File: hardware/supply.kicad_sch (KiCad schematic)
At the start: 13 parts, among them U4 LMR51610XDBVR

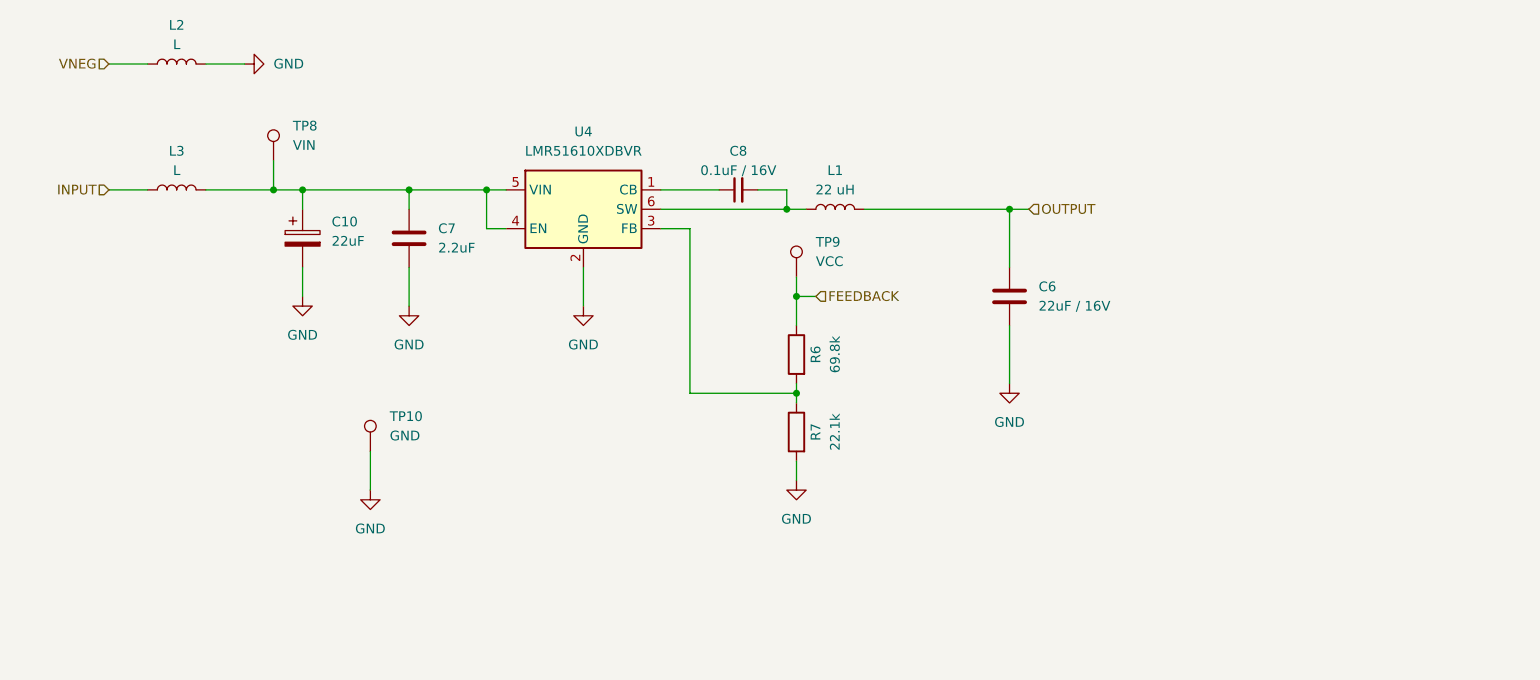
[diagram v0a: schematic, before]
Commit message: Remove PLC, use ESP
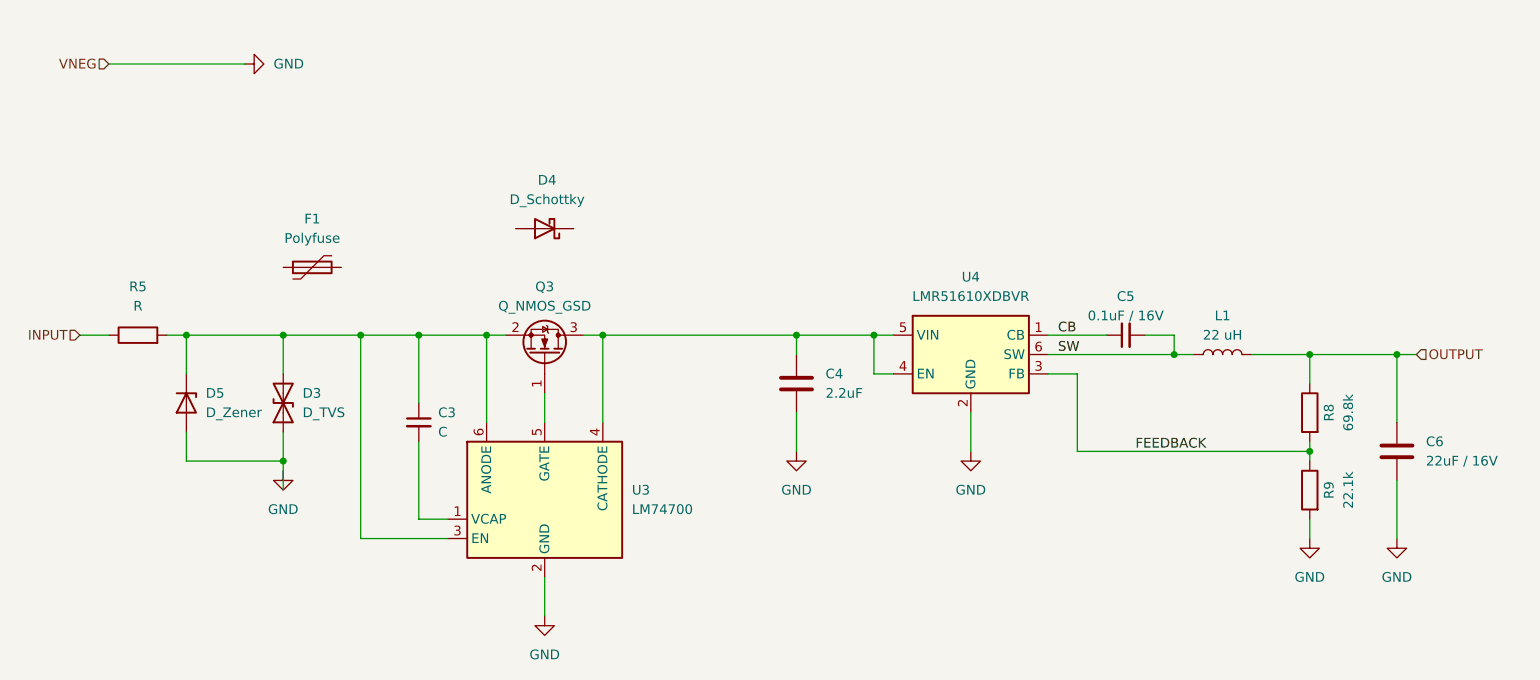
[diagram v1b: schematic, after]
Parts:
- removed C10: 22uF, Capacitor_SMD:CP_Elec_8x10, symbol Device:C_Polarized
- removed L2, L3: L, Inductor_SMD:L_2512_6332Metric_Pad1.52x3.35mm_HandSolder, symbol Device:L
- removed TP10: GND, TestPoint:TestPoint_Loop_D2.50mm_Drill1.0mm, symbol Connector:TestPoint
- removed TP8: VIN, TestPoint:TestPoint_Loop_D2.50mm_Drill1.0mm, symbol Connector:TestPoint
- removed TP9: VCC, TestPoint:TestPoint_Loop_D2.50mm_Drill1.0mm, symbol Connector:TestPoint
- added C3: C, Capacitor_SMD:C_1206_3216Metric_Pad1.33x1.80mm_HandSolder, symbol Device:C_Small
- added D3: D_TVS, symbol Device:D_TVS
- added D4: D_Schottky, symbol Device:D_Schottky
- added D5: D_Zener, symbol Device:D_Zener
- added F1: Polyfuse, symbol Device:Polyfuse
- added Q3: Q_NMOS_GSD, Package_TO_SOT_SMD:TSOT-23_HandSoldering, symbol Device:Q_NMOS_GSD
- added R5: R, symbol Device:R
- added U3: LM74700, Package_TO_SOT_SMD:SOT-23-6, symbol Power_Management:LM74700
- U4: symbol lmr51606:LMR51606 -> symbols:LMR51610
- renumbered C7 to C4, C8 to C5, R6 to R8, R7 to R9
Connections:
- net FEEDBACK: now also R8.2, R9.1, U4.3 (FB); no longer R8.1
- net GND: now also U3.2 (GND)
- net INPUT: now also R5.1
- net OUTPUT: now also R8.1
- net CB: now reaches C5.1, U4.1 (CB)
- net SW: now reaches C5.2, L1.1, U4.6 (SW)
- net at C4.1, U4.4 (EN), U4.5 (VIN): now also Q3.3 (D), U3.4 (CATHODE)
- new net: Q3.1 (G), U3.5 (GATE)
- new net: C3.1, D3.2 (A2), D5.1 (K), Q3.2 (S), R5.2, U3.3 (EN), U3.6 (ANODE)
- new net: D3.1 (A1), D5.2 (A)
- new net: C3.2, U3.1 (VCAP)
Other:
- moved on the sheet: C4, C5, C6, L1, R8, R9, U4

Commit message: rev 1
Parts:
- removed C3: C, Capacitor_SMD:C_1206_3216Metric_Pad1.33x1.80mm_HandSolder, symbol Device:C_Small
- removed D3: D_TVS, symbol Device:D_TVS
- removed D4: D_Schottky, symbol Device:D_Schottky
- removed D5: D_Zener, symbol Device:D_Zener
- removed F1: Polyfuse, symbol Device:Polyfuse
- removed Q3: Q_NMOS_GSD, Package_TO_SOT_SMD:TSOT-23_HandSoldering, symbol Device:Q_NMOS_GSD
- removed R5: R, symbol Device:R
- removed U3: LM74700, Package_TO_SOT_SMD:SOT-23-6, symbol Power_Management:LM74700
- added C5: 0.1uF, Capacitor_SMD:C_0603_1608Metric_Pad1.08x0.95mm_HandSolder, symbol Device:C
- C7: renamed from C5; footprint Capacitor_SMD:C_1206_3216Metric_Pad1.33x1.80mm_HandSolder -> Capacitor_SMD:C_0603_1608Metric_Pad1.08x0.95mm_HandSolder
- C8: renamed from C6; footprint Capacitor_SMD:C_1210_3225Metric_Pad1.33x2.70mm_HandSolder -> Capacitor_SMD:C_1206_3216Metric_Pad1.33x1.80mm_HandSolder
- renumbered C4 to C6, R9 to R11, R8 to R9, U4 to U3
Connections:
- net GND: now also C5.2
- net INPUT: now also C6.1, U3.4 (EN), U3.5 (VIN), C5.1
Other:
- moved on the sheet: C6

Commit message: Improve BOM
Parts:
- C5, C6: Characteristics (none) -> 100V
- C7: value 0.1uF / 16V -> 0.1uF; Characteristics (none) -> 16V
- C8: value 22uF / 16V -> 10uF; Characteristics (none) -> 16V
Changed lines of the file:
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@@
 			)
 		)
-		(property "Value" "0.1uF / 16V"
+		(property "Value" "0.1uF"
 			(at 168.91 100.33 90)
 			(effects
@@
 		(property "Description" "Unpolarized capacitor, small symbol"
 			(at 168.91 102.87 0)
+			(effects
+				(font
+					(size 1.27 1.27)
+				)
+				(hide yes)
+			)
+		)
+		(property "Characteristics" "16V"
+			(at 168.91 102.87 90)
 			(effects
 				(font
@@
 			)
 		)
-		(property "Value" "22uF / 16V"
+		(property "Value" "10uF"
 			(at 208.28 119.38 0)
 			(effects
@@
 		)
 		(property "Description" "Unpolarized capacitor"
+			(at 204.47 118.11 0)
+			(effects
+				(font
+					(size 1.27 1.27)
+				)
+				(hide yes)
+			)
+		)
+		(property "Characteristics" "16V"
 			(at 204.47 118.11 0)
 			(effects
@@
 		(on_board yes)
 		(dnp no)
-		(fields_autoplaced yes)
 		(property "Reference" "C6"
-			(at 119.38 107.95 0)
+			(at 119.38 107.9499 0)
 			(effects
 				(font
@@
 		)
 		(property "Value" "2.2uF"
-			(at 119.38 110.49 0)
+			(at 119.38 110.4899 0)
 			(effects
 				(font
@@
 				)
 				(hide yes)
+			)
+		)
+		(property "Characteristics" "100V"
+			(at 119.38 112.776 0)
+			(effects
+				(font
+					(size 1.27 1.27)
+				)
+				(justify left)
 			)
 		)
@@
 		(on_board yes)
 		(dnp no)
-		(fields_autoplaced yes)
 		(property "Reference" "C5"
 			(at 132.08 107.9499 0)
@@
 			)
 		)
+		(property "Characteristics" "100V"
+			(at 132.08 112.776 0)
+			(effects
+				(font
+					(size 1.27 1.27)
+				)
+				(justify left)
+			)
+		)
